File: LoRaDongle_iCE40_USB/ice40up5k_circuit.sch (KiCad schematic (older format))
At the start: 23 parts

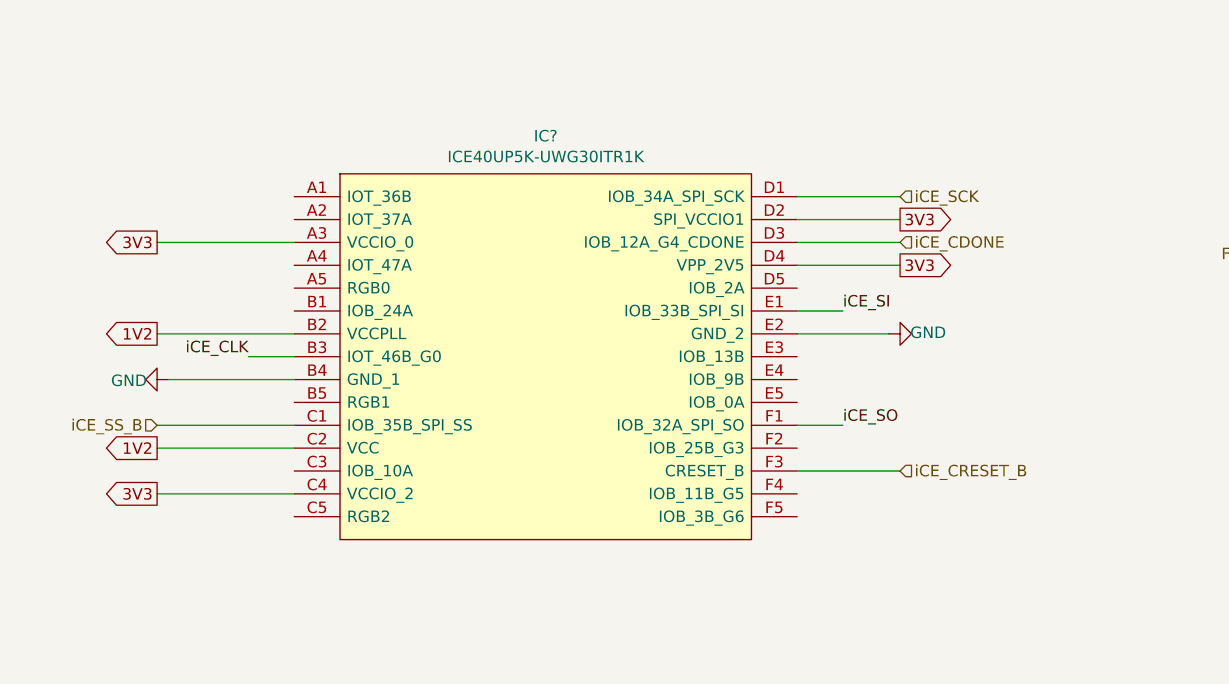
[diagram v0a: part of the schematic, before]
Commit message: connected FPGA to SX1261
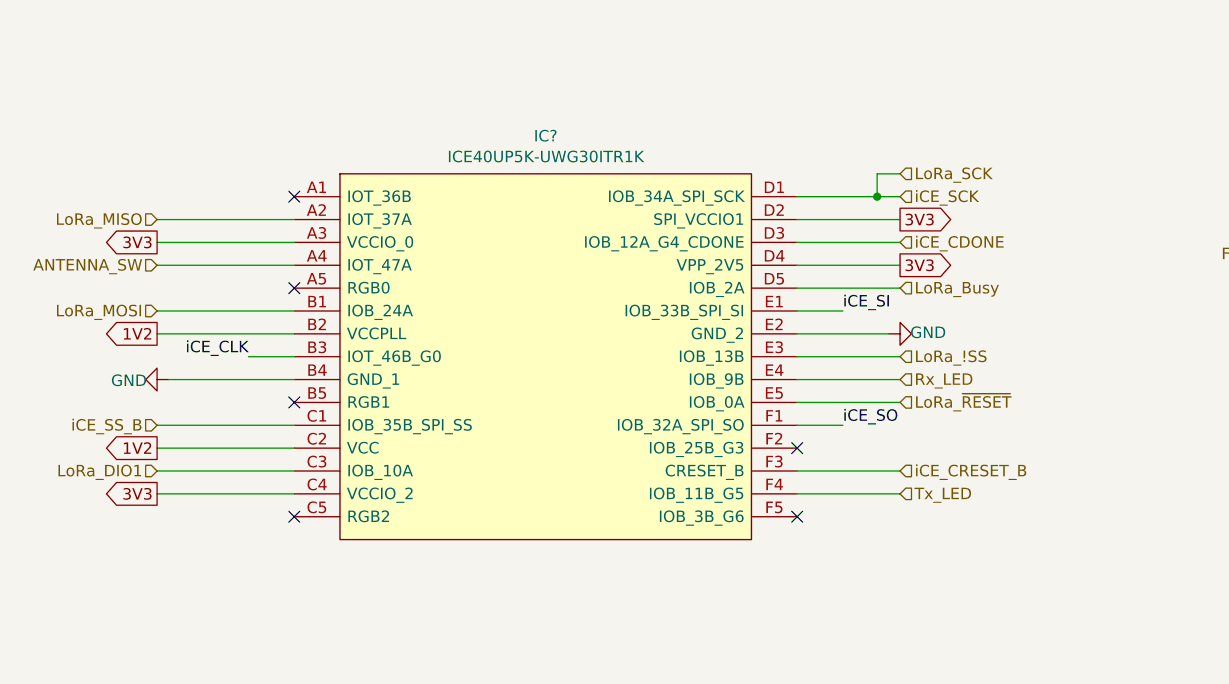
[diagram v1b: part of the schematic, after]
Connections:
- net LoRa_MISO: now reaches IC?.A2 (IOT_37A)
- net ANTENNA_SW: now reaches IC?.A4 (IOT_47A)
- net LoRa_MOSI: now reaches IC?.B1 (IOB_24A)
- net LoRa_DIO1: now reaches IC?.C3 (IOB_10A)
- net LoRa_Busy: now reaches IC?.D5 (IOB_2A)
- net LoRa_!SS: now reaches IC?.E3 (IOB_13B)
- net Rx_LED: now reaches IC?.E4 (IOB_9B)
- net LoRa_~RESET: now reaches IC?.E5 (IOB_0A)
- net Tx_LED: now reaches IC?.F4 (IOB_11B_G5)
- net iCE_SCK renamed LoRa_SCK
- no-connect marks 1 -> 7

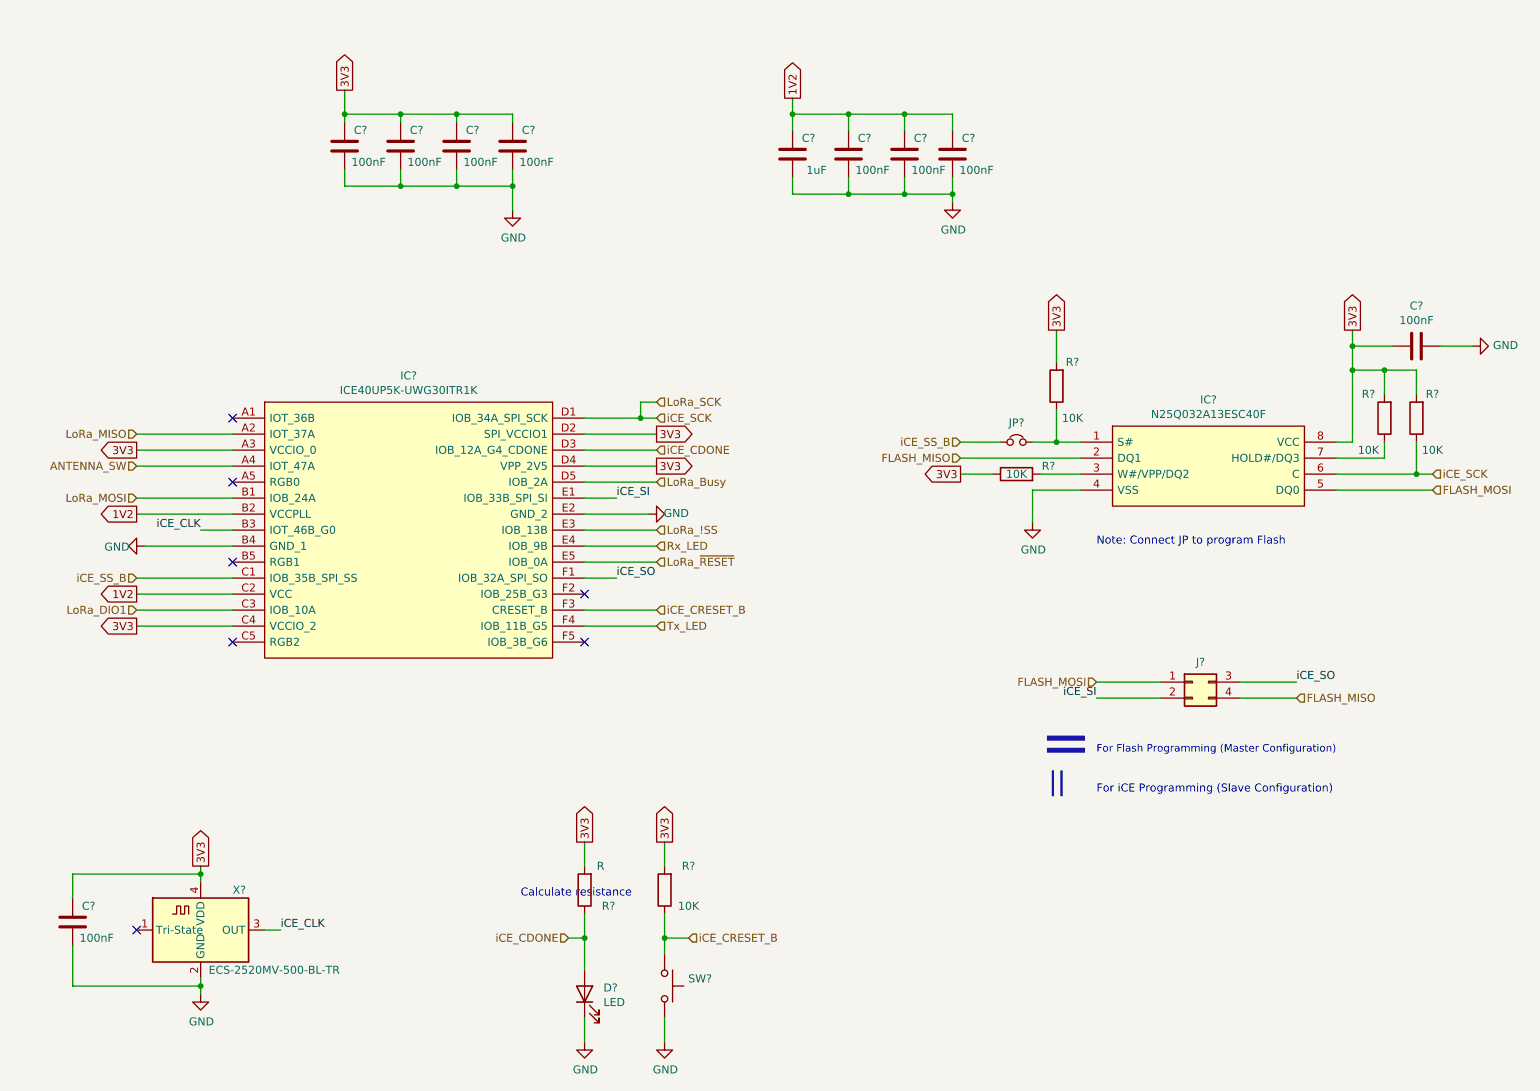
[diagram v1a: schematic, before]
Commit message: added footprints
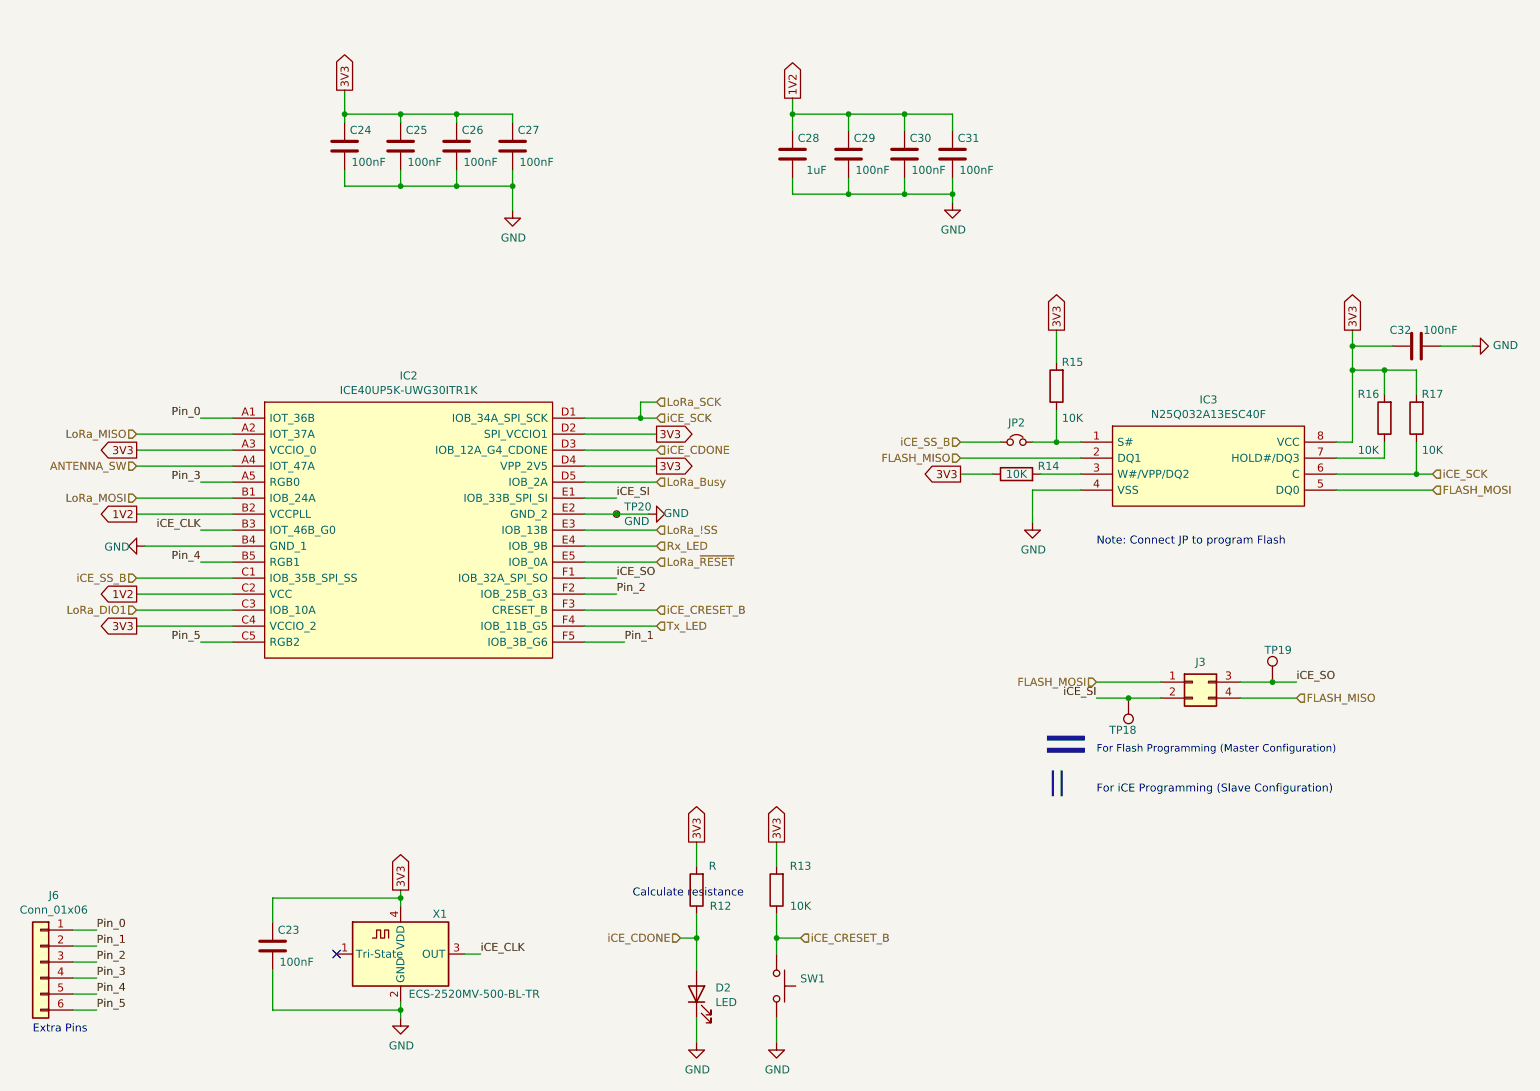
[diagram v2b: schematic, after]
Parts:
- removed C? (x8): 100nF, symbol Device:C
- added C24, C25, C26, C27, C29, C30, C31, C32: 100nF, Capacitor_SMD:C_01005_0402Metric, symbol Device:C
- added J6: Conn_01x06, Connector_PinHeader_2.54mm:PinHeader_1x06_P2.54mm_Vertical, symbol Connector_Generic:Conn_01x06
- added TP18: iCE_SI, TestPoint:TestPoint_Pad_D2.5mm, symbol Connector:TestPoint
- added TP19: iCE_SO, TestPoint:TestPoint_Pad_D2.5mm, symbol Connector:TestPoint
- added TP20: GND, TestPoint:TestPoint_Pad_D2.5mm, symbol Connector:TestPoint_Small
- C23: renamed from C?; footprint (none) -> Capacitor_SMD:C_01005_0402Metric; Part Number (none) -> GRM155R71C104KA88D
- C28: renamed from C?; footprint (none) -> Capacitor_SMD:C_01005_0402Metric; Part Number (none) -> GRM155R70J105MA12D
- D2: renamed from D?; footprint (none) -> LED_SMD:LED_0603_1608Metric
- IC2: renamed from IC?; footprint BGA30C40P5X6_211X254X60 -> ICE40UP5K-UWG30ITR1K_KiCad:BGA30C40P5X6_211X254X60
- IC3: renamed from IC?; footprint SOIC127P600X175-8N -> N25Q032A13ESC40F:SOIC127P600X175-8N
- J3: renamed from J?; footprint Connector_PinHeader_1.00mm:PinHeader_2x02_P1.00mm_Vertical -> Connector_PinHeader_2.54mm:PinHeader_2x02_P2.54mm_Vertical
- JP2: renamed from JP?; footprint (none) -> Connector_PinHeader_2.54mm:PinHeader_1x02_P2.54mm_Vertical
- R12, R13, R14, R15, R16, R17: renamed from R?; footprint (none) -> Resistor_SMD:R_0402_1005Metric
- SW1: renamed from SW?; footprint (none) -> Button_Switch_THT:SW_PUSH_6mm_H5mm
- gave numbers to parts that had none: 1
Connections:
- net 1V2: now also C29.2, C30.2, C31.2
- net 3V3: now also C24.2, C25.2, C26.2, C27.2, C32.2
- net GND: now also C24.1, C25.1, C26.1, C27.1, C29.1, C30.1, C31.1, C32.1, TP20.1
- net iCE_SI: now also TP18.1
- net iCE_SO: now also TP19.1
- net Pin_0: now reaches IC2.A1 (IOT_36B)
- net Pin_0: now also J6.1 (Pin_1)
- net Pin_3: now reaches IC2.A5 (RGB0)
- net Pin_3: now also J6.4 (Pin_4)
- net Pin_4: now reaches IC2.B5 (RGB1)
- net Pin_4: now also J6.5 (Pin_5)
- net Pin_5: now reaches IC2.C5 (RGB2)
- net Pin_5: now also J6.6 (Pin_6)
- net Pin_2: now reaches IC2.F2 (IOB_25B_G3)
- net Pin_2: now also J6.3 (Pin_3)
- net Pin_1: now reaches IC2.F5 (IOB_3B_G6)
- net Pin_1: now also J6.2 (Pin_2)
- no-connect marks 7 -> 1
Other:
- note added: "Extra Pins"
- moved on the sheet: C23, D2, R12, R13, SW1, X1

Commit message: PCB Layout V01
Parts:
- added J9: Conn_02x02_Top_Bottom, Connector_PinHeader_2.54mm:PinHeader_2x02_P2.54mm_Vertical, symbol Connector_Generic:Conn_02x02_Top_Bottom
- C23, C24, C25, C26, C27, C28, C29, C30, C31, C32: footprint Capacitor_SMD:C_01005_0402Metric -> Capacitor_SMD:C_0402_1005Metric_Pad0.74x0.62mm_HandSolder
- D2: value LED -> Done; footprint LED_SMD:LED_0603_1608Metric -> LED_SMD:LED_0603_1608Metric_Pad1.05x0.95mm_HandSolder
- GND3: renamed from TP20; footprint TestPoint:TestPoint_Pad_D2.5mm -> TestPoint:TestPoint_Pad_D1.0mm
- R12, R13, R14, R15, R16, R17: footprint Resistor_SMD:R_0402_1005Metric -> Resistor_SMD:R_0402_1005Metric_Pad0.72x0.64mm_HandSolder
- iCE_SI1: renamed from TP18; footprint TestPoint:TestPoint_Pad_D2.5mm -> TestPoint:TestPoint_Pad_D1.0mm
- iCE_SO1: renamed from TP19; footprint TestPoint:TestPoint_Pad_D2.5mm -> TestPoint:TestPoint_Pad_D1.0mm
- renumbered JP2 to J7
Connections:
- net 1V2: now also J9.2 (Pin_2); no longer C28.2, C29.2, C30.2, C31.2, IC2.B2 (VCCPLL), IC2.C2 (VCC)
- net 3V3: now also J9.1 (Pin_1); no longer C24.2, C25.2, C26.2, C27.2, IC2.A3 (VCCIO_0), IC2.C4 (VCCIO_2), IC2.D2 (SPI_VCCIO1), IC2.D4 (VPP_2V5)
- net iCE_SS_B: now also J7.2; no longer J7.1
- net at IC3.1 (S#), R15.1: now also J7.1; no longer J7.2
- new net 1V2FPGA: C28.2, C29.2, C30.2, C31.2, IC2.B2 (VCCPLL), IC2.C2 (VCC), J9.4 (Pin_4)
- new net 3V3FPGA: C24.2, C25.2, C26.2, C27.2, IC2.A3 (VCCIO_0), IC2.C4 (VCCIO_2), IC2.D2 (SPI_VCCIO1), IC2.D4 (VPP_2V5), J9.3 (Pin_3)
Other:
- moved on the sheet: C24, C25, C26, C27, J7
